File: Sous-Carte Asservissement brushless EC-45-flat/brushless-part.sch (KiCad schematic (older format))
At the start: 13 parts, among them K1 Maxon-200142, K2 Maxon-200142, U2 DEC24/2, U3 DEC24/2

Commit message: asser 1A : BOM + ready for pisa !
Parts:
- C1: footprint Capacitors_SMD:c_elec_6.3x4.5 -> Capacitors_SMD:c_elec_6.3x7.7; manf# (none) -> EMVE250ADA101MF80G
- D1, D2: manf# (none) -> MBR0530T1G
- F1, F2: manf# (none) -> MF-R300
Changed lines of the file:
@@
 F 2 "Fuse_Holders_and_Fuses:Fuse_TE5_Littlefuse-395Series" H 3950 1850 50  0001 C CNN
 F 3 "" H 3950 1850 50  0000 C CNN
+F 4 "MF-R300" H 3950 1850 60  0001 C CNN "manf#"
 	1    3950 1850
 	1    0    0    -1
@@
 F 2 "Diodes_SMD:SOD-123" H 5000 2050 50  0001 C CNN
 F 3 "http://www.farnell.com/datasheets/85890.pdf" H 5000 2050 50  0001 C CNN
+F 4 "MBR0530T1G" V 5000 2050 60  0001 C CNN "manf#"
 	1    5000 2050
 	0    1    1    0
@@
 F 0 "C1" H 1888 2096 50  0000 L CNN
 F 1 "100u/35v EEEHA1V101XP" H 1888 2005 50  0000 L CNN
-F 2 "Capacitors_SMD:c_elec_6.3x4.5" H 1800 2050 50  0001 C CNN
+F 2 "Capacitors_SMD:c_elec_6.3x7.7" H 1800 2050 50  0001 C CNN
 F 3 "" H 1800 2050 50  0000 C CNN
+F 4 "EMVE250ADA101MF80G" H 1800 2050 60  0001 C CNN "manf#"
 	1    1800 2050
 	1    0    0    -1
@@
 F 2 "Fuse_Holders_and_Fuses:Fuse_TE5_Littlefuse-395Series" H 3950 4200 50  0001 C CNN
 F 3 "" H 3950 4200 50  0000 C CNN
+F 4 "MF-R300" H 3950 4200 60  0001 C CNN "manf#"
 	1    3950 4200
 	1    0    0    -1
@@
 F 2 "Diodes_SMD:SOD-123" H 5000 4400 50  0001 C CNN
 F 3 "http://www.farnell.com/datasheets/85890.pdf" H 5000 4400 50  0001 C CNN
+F 4 "MBR0530T1G" V 5000 4400 60  0001 C CNN "manf#"
 	1    5000 4400
 	0    1    1    0

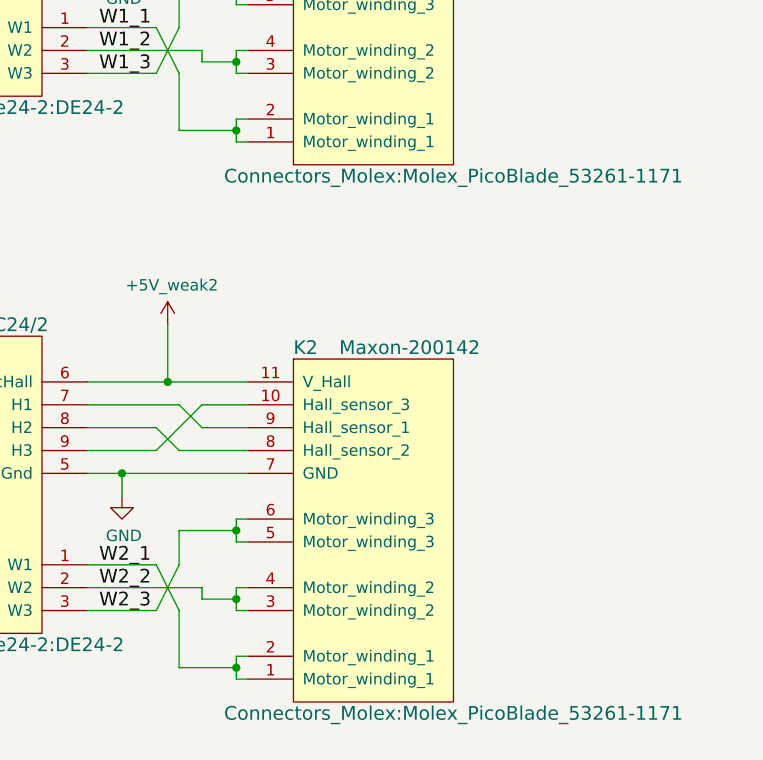
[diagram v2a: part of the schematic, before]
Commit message: asser 1A : corrected zif sockets
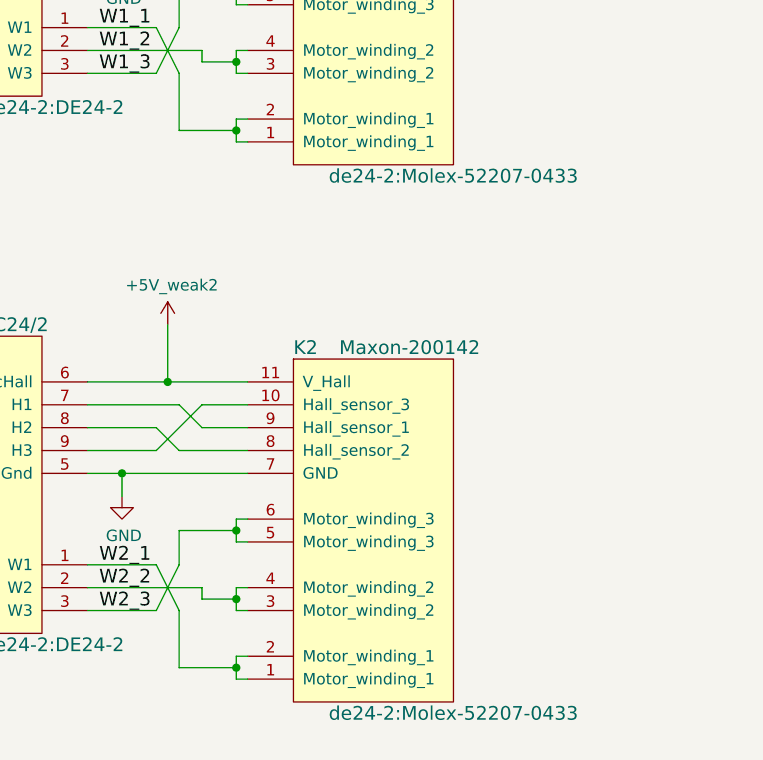
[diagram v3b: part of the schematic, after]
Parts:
- K1, K2: footprint Connectors_Molex:Molex_PicoBlade_53261-1171 -> de24-2:Molex-52207-0433
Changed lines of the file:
@@
 F 0 "K1" H 8800 2900 60  0000 L CNN
 F 1 "Maxon-200142" H 9000 2900 60  0000 L CNN
-F 2 "Connectors_Molex:Molex_PicoBlade_53261-1171" H 9500 1300 60  0000 C CNN
+F 2 "de24-2:Molex-52207-0433" H 9500 1300 60  0000 C CNN
 F 3 "" H 8700 2650 60  0000 C CNN
 	1    9200 2550
@@
 F 0 "K2" H 8800 5250 60  0000 L CNN
 F 1 "Maxon-200142" H 9000 5250 60  0000 L CNN
-F 2 "Connectors_Molex:Molex_PicoBlade_53261-1171" H 9500 3650 60  0000 C CNN
+F 2 "de24-2:Molex-52207-0433" H 9500 3650 60  0000 C CNN
 F 3 "" H 8700 5000 60  0000 C CNN
 	1    9200 4900
